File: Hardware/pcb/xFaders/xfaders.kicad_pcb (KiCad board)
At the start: 2 copper layers, 100.3 x 57.1 mm, 32 parts, among them J1 Conn_01x03_Male, J10 Conn_01x03_Male, J11 Conn_01x03_Male, J12 Conn_01x03_Male, J13 Conn_01x03_Male, J14 Conn_01x03_Male, J15 Conn_01x03_Male, J16 Conn_02x10_Odd_Even, J17 Conn_02x10_Odd_Even, J18 Conn_02x10_Odd_Even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

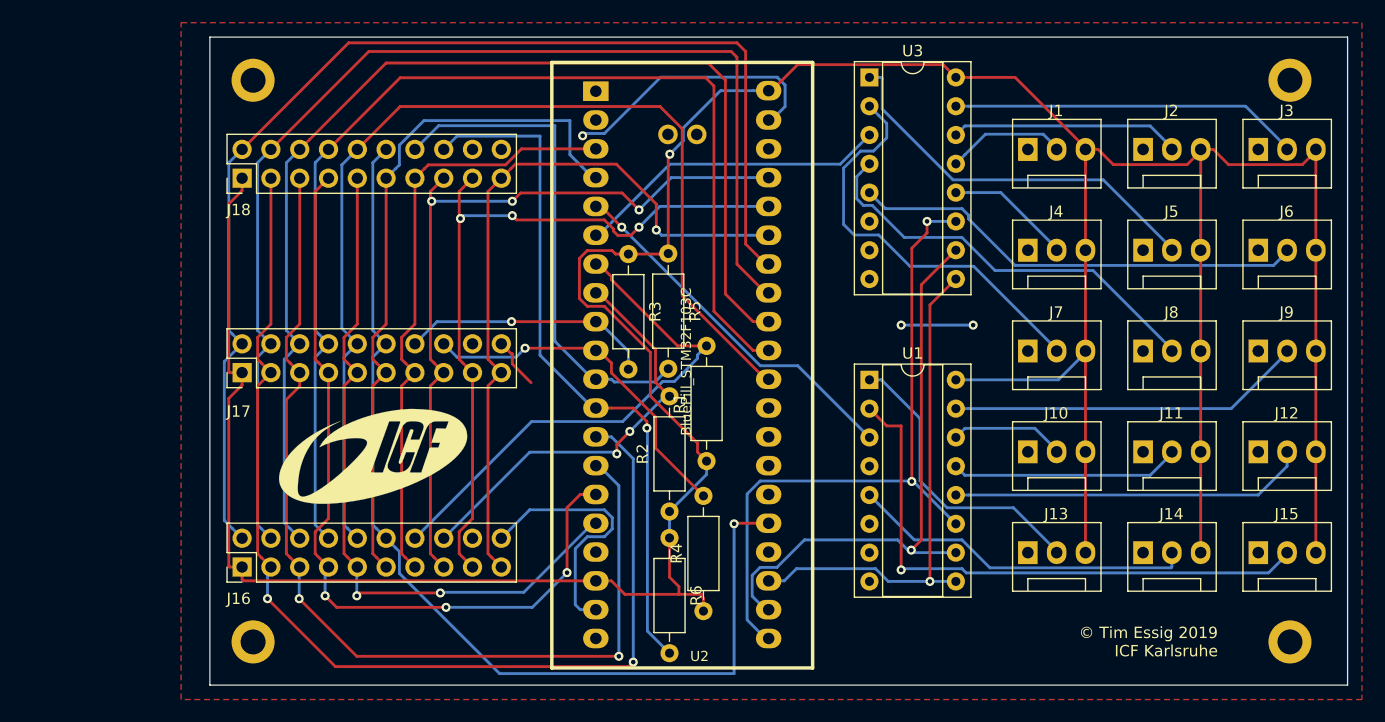
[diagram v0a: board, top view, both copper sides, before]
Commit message: Update PCB for new RGB LEDs and 5V power supply
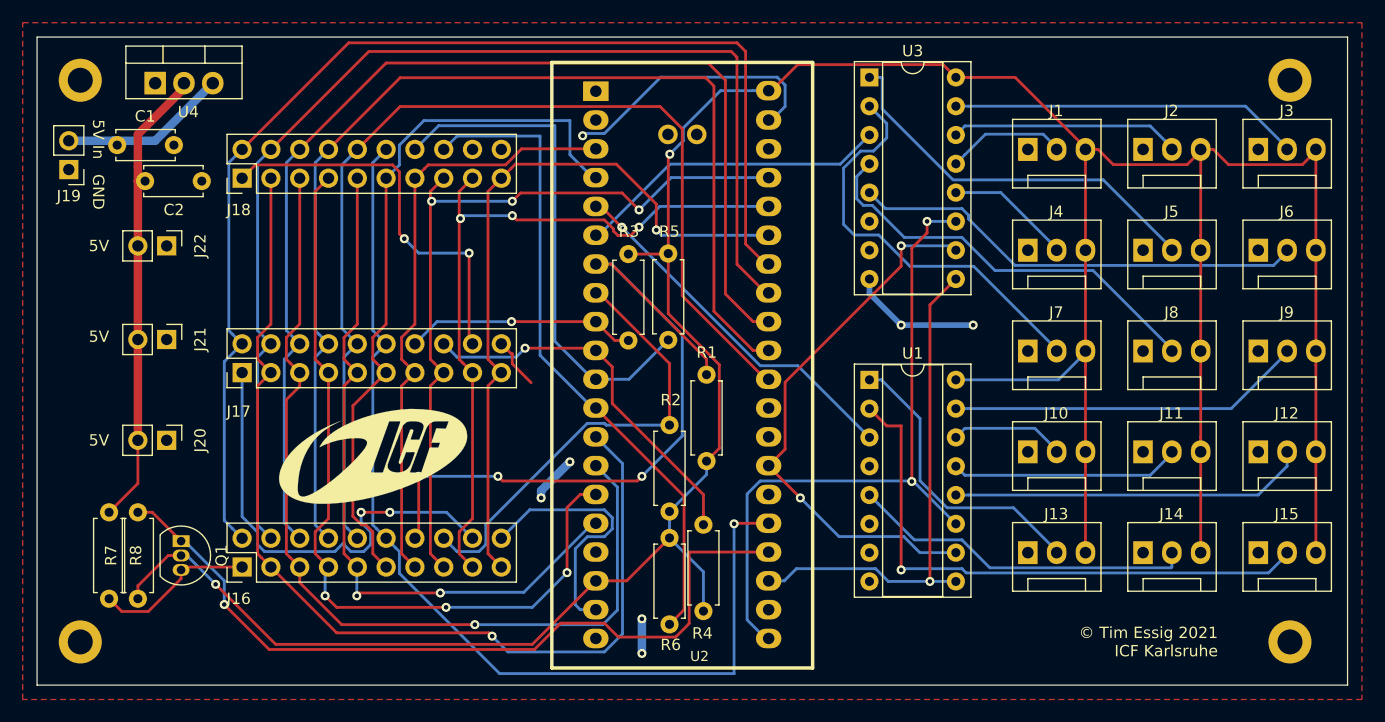
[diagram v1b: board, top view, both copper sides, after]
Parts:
- added C1: 10 uF, Capacitor_THT:C_Disc_D5.0mm_W2.5mm_P5.00mm, F.Cu at (61.9, 68.2)
- added C2: 10 uF, Capacitor_THT:C_Disc_D5.0mm_W2.5mm_P5.00mm, F.Cu at (64.4, 71.4)
- added J19: PWR In, Connector_PinHeader_2.54mm:PinHeader_1x02_P2.54mm_Vertical, F.Cu at (57.7, 70.4)
- added J20: 5V, Connector_PinHeader_2.54mm:PinHeader_1x02_P2.54mm_Vertical, F.Cu at (66.3, 94.2)
- added J21: 5V, Connector_PinHeader_2.54mm:PinHeader_1x02_P2.54mm_Vertical, F.Cu at (66.3, 85.3)
- added J22: 5V, Connector_PinHeader_2.54mm:PinHeader_1x02_P2.54mm_Vertical, F.Cu at (66.3, 77.1)
- added Q1: 2N7000, Package_TO_SOT_THT:TO-92_Inline, F.Cu at (67.6, 103.1)
- added R7: 10k, Resistor_THT:R_Axial_DIN0207_L6.3mm_D2.5mm_P7.62mm_Horizontal, F.Cu at (63.8, 108.2)
- added R8: 10k, Resistor_THT:R_Axial_DIN0207_L6.3mm_D2.5mm_P7.62mm_Horizontal, F.Cu at (61.2, 100.6)
- added U4: LM1084-5.0, Package_TO_SOT_THT:TO-220-3_Vertical, F.Cu at (65.3, 62.7)
- R1, R2, R3, R4, R5, R6: footprint Resistor_THT:R_Axial_DIN0207_L6.3mm_D2.5mm_P10.16mm_Horizontal -> Resistor_THT:R_Axial_DIN0207_L6.3mm_D2.5mm_P7.62mm_Horizontal
- moved REF** 15.2 mm to (58.7, 62.5)
- moved REF** 15.2 mm to (58.7, 112.0)
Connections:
- J16 pad 1: VCC3V3 -> SPI_5V
- J17 pad 1: VCC3V3 -> Net-(J16-Pad18)
- J18 pad 1: VCC3V3 -> Net-(J17-Pad18)
- J18 pad 18: Net-(J18-Pad18) -> (no net)
- U1 pad 4: Net-(U1-Pad4) -> (no net)
- U2 pad 1: Net-(U2-Pad1) -> (no net)
- U2 pad 17: Net-(U2-Pad17) -> (no net)
- U2 pad 2: Net-(U2-Pad2) -> (no net)
- U2 pad 22: Net-(U1-Pad10) -> (no net)
- U2 pad 24: Net-(U2-Pad24) -> SPI_3V3
- U2 pad 26: Net-(U2-Pad26) -> (no net)
- U2 pad 27: Net-(U2-Pad27) -> Net-(U1-Pad10)
- U2 pad 28: Net-(U2-Pad28) -> (no net)
- U2 pad 29: Net-(U2-Pad29) -> (no net)
- U2 pad 38: Net-(U2-Pad38) -> (no net)
- U2 pad 41: Net-(U2-Pad41) -> (no net)
- U2 pad 42: Net-(U2-Pad42) -> (no net)
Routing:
- net SPI_3V3: track 0.00 -> 70.1 mm, vias 0 -> 1
- net VCC5V: track 0.00 -> 41.2 mm
- net Net-(J16-Pad18): track 0.00 -> 41.0 mm, vias 0 -> 2
- net Net-(J17-Pad18): track 0.00 -> 35.1 mm, vias 0 -> 2
- net VCC3V3: track 320.9 -> 290.8 mm, vias 1 -> 2
- net Row0: track 45.8 -> 64.4 mm, vias 0 -> 3
- net Net-(C1-Pad1): track 0.00 -> 15.8 mm
- net SPI_5V: track 0.00 -> 14.3 mm
- net GND: track 58.1 -> 70.5 mm, vias 3 -> 7
- net Col0: track 96.1 -> 89.4 mm, vias 2 -> 1
- net Col1: track 87.2 -> 81.2 mm, vias 2 -> 1
- net Row5: track 61.4 -> 58.0 mm, vias 1 -> 0
- net Row1: track 37.7 -> 40.7 mm, vias 2 -> 0
- net Net-(U1-Pad10): track 51.6 -> 48.9 mm, vias 1 -> 2
- net Row3: track 31.2 -> 33.6 mm
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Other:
- board size 100.3 x 57.1 mm -> 115.6 x 57.1 mm
- board text added: "5V"
- board text added: "5V In GND"
- board text added: "© Tim Essig 2021 ICF Karlsruhe"
- board text removed: "© Tim Essig 2019 ICF Karlsruhe"
